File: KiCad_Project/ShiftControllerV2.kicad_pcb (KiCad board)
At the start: 2 copper layers, 20 parts, among them J1 SOLENOID, J2 PWR + I/O, Q1 BTN8982TA, Q2 BTN8982TA, U1 ControllerBoardV1

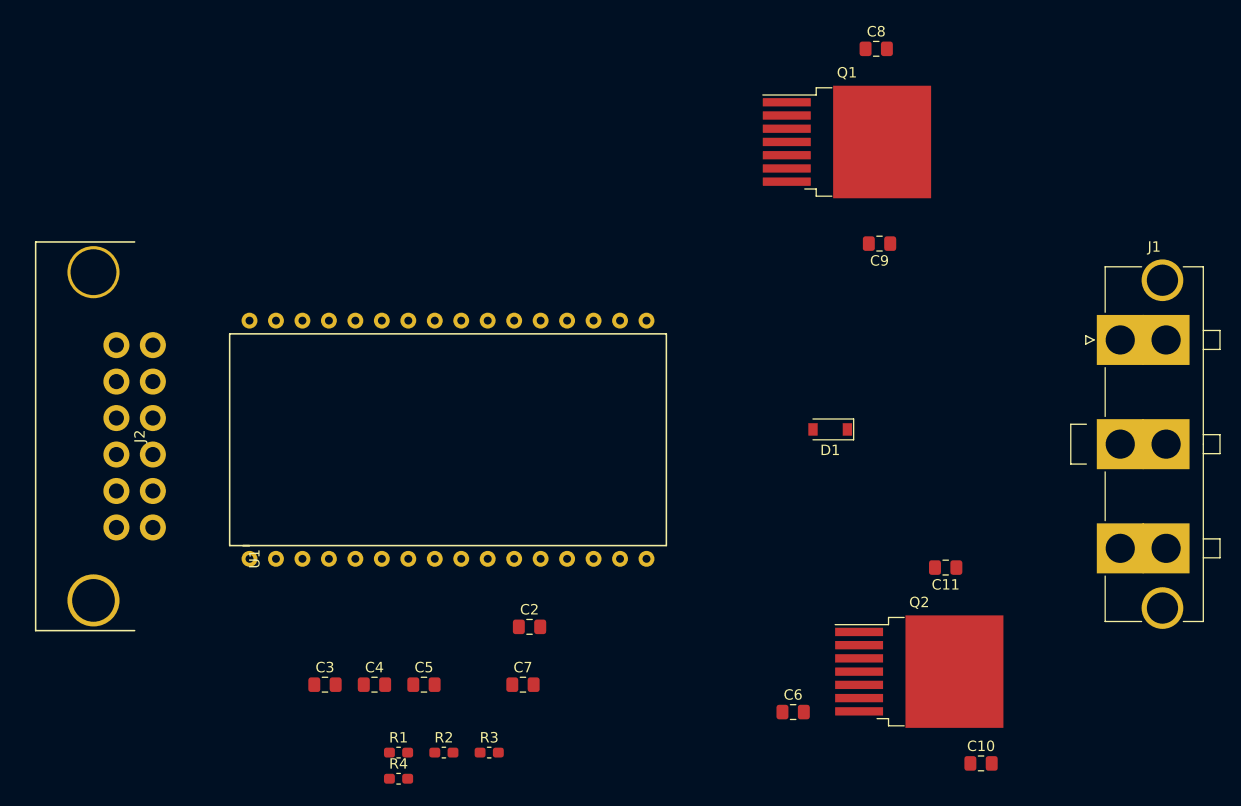
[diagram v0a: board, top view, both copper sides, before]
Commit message: Began planning arrangement of components
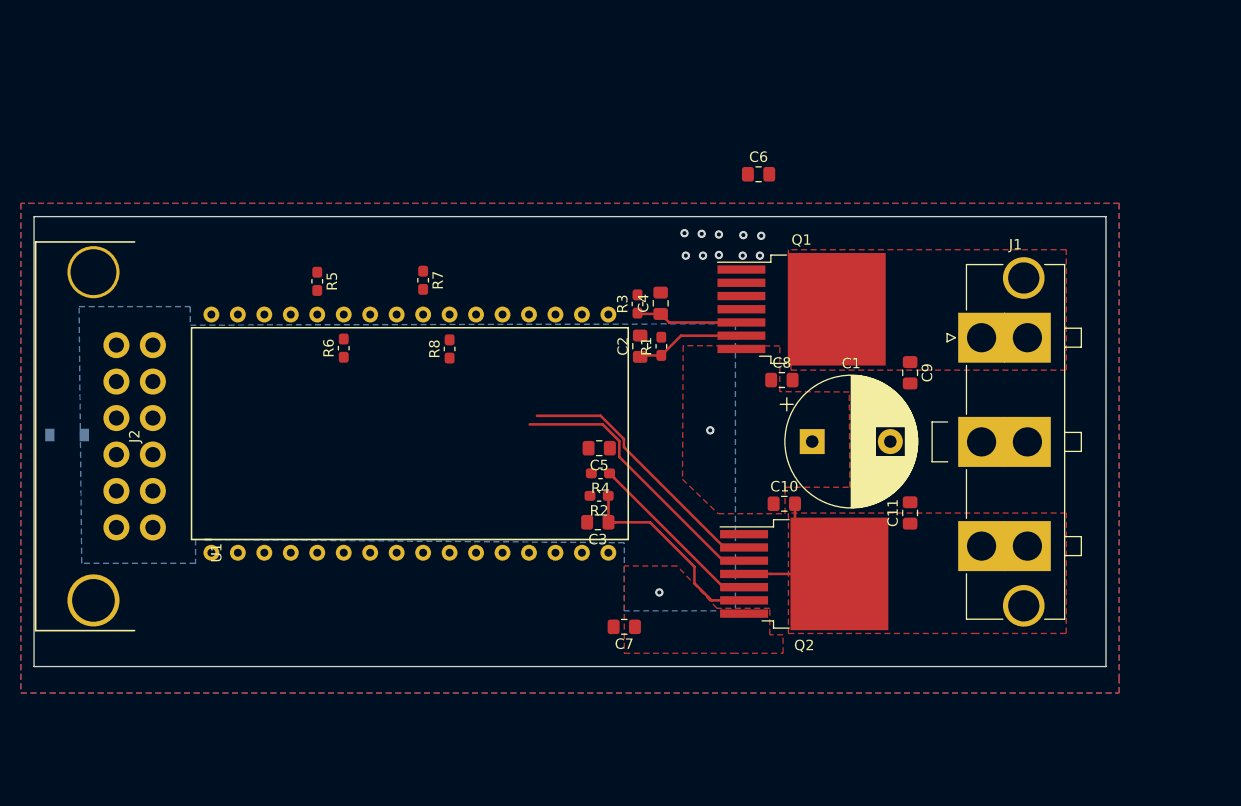
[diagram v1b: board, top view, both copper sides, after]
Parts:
- added C1: 1000u, Capacitor_THT:CP_Radial_D12.5mm_P7.50mm, F.Cu at (150.9, 97.8)
- added R5: 10k, Resistor_SMD:R_0603_1608Metric_Pad1.05x0.95mm_HandSolder, F.Cu at (103.4, 82.4)
- added R6: 10k, Resistor_SMD:R_0603_1608Metric_Pad1.05x0.95mm_HandSolder, F.Cu at (105.9, 88.8)
- added R7: 10k, Resistor_SMD:R_0603_1608Metric_Pad1.05x0.95mm_HandSolder, F.Cu at (113.5, 82.3)
- added R8: 10k, Resistor_SMD:R_0603_1608Metric_Pad1.05x0.95mm_HandSolder, F.Cu at (116.1, 88.9)
- C3: value 100n -> 1n
- D1: value 30v -> 30v zener; moved to B.Cu
- moved D1 73.2 mm to (79.4, 97.2)
- moved C6 51.7 mm to (145.7, 72.1)
- moved R1 46.4 mm to (136.4, 88.6), turned to 90 degrees
- moved C4 45.8 mm to (136.3, 84.5), turned to 90 degrees
- moved R3 45.3 mm to (134.1, 84.6), turned to 90 degrees
- moved R4 35.1 mm to (130.6, 100.8), turned to 180 degrees
- moved C8 33.1 mm to (148.0, 91.9)
- moved C10 31.3 mm to (148.2, 103.8)
- moved C3 30.5 mm to (130.3, 105.5), turned to 180 degrees
- moved C2 29.0 mm to (134.4, 88.6), turned to 90 degrees
- moved R2 28.8 mm to (130.4, 103.0), turned to 180 degrees
- moved C5 28.2 mm to (130.4, 98.4), turned to 180 degrees
- moved Q1 16.6 mm to (149.9, 85.1)
- moved Q2 14.5 mm to (150.1, 110.5)
- moved J1 13.3 mm to (167.1, 87.8)
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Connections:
- J2 pad 3: CANH -> CANL
- J2 pad 4: CANL -> CANH
- Q1 pad 2: (no net) -> IN1
- Q1 pad 3: (no net) -> INH1
- Q2 pad 2: (no net) -> IN2
- Q2 pad 3: (no net) -> INH2
- U1 pad 21: (no net) -> Net-(R5-Pad2)
- U1 pad 22: (no net) -> Net-(R6-Pad2)
- U1 pad 23: CURRENT1 -> CURRENT2
- U1 pad 24: CURRENT2 -> CURRENT1
- U1 pad 25: (no net) -> Net-(R7-Pad2)
- U1 pad 26: (no net) -> Net-(R8-Pad2)
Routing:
- net INH2: track 0.00 -> 26.9 mm
- net IN2: track 0.00 -> 25.6 mm
- net CURRENT2: track 0.00 -> 19.6 mm
- net OUT2: track 0.00 -> 17.6 mm
- net Net-(C5-Pad1): track 0.00 -> 17.4 mm
- net CURRENT1: track 0.00 -> 10.6 mm
- net Net-(C4-Pad1): track 0.00 -> 10.3 mm
- net INH1: track 0.00 -> 1.90 mm
- net IN1: track 0.00 -> 1.90 mm
- net GND: vias 0 -> 10
- net +12V: vias 0 -> 2
- added copper zone on B.Cu, net +12V
- added copper zone on F.Cu, net +12V
- added copper zone on B.Cu, net GND
- added copper zone on F.Cu, net GND
- added copper zone on F.Cu, net OUT1
- added copper zone on F.Cu, net OUT2
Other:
- board outline added: 102.9 x 43.2 mm

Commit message: Layout almost complete
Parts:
- removed C2: 1n, Capacitor_SMD:C_0805_2012Metric_Pad1.15x1.40mm_HandSolder
- added Ce: 1n, Capacitor_SMD:C_0603_1608Metric_Pad1.05x0.95mm_HandSolder, F.Cu at (135.5, 81.3)
- C10, C11, C3, C4, C5, C6, C7, C8, C9: footprint Capacitor_SMD:C_0805_2012Metric_Pad1.15x1.40mm_HandSolder -> Capacitor_SMD:C_0603_1608Metric_Pad1.05x0.95mm_HandSolder
- D1: moved to F.Cu
- J1: value SOLENOID -> Conn_02x06_Top_Bottom; footprint Connector_Molex:Molex_Mini-Fit_Sr_42819-32XX_1x03_P10.00mm_Vertical -> Lukas_Library:MX120G
- J2: value PWR + I/O -> Conn_02x06_Top_Bottom
- R5, R6, R7, R8: moved to B.Cu
- moved C6 16.4 mm to (135.4, 85.0), turned to 180 degrees
- moved D1 14.8 mm to (90.8, 87.7), turned to 135 degrees
- moved C5 13.4 mm to (135.1, 111.0)
- moved R2 13.0 mm to (135.4, 115.1)
- moved J1 11.7 mm to (173.2, 97.8), turned to 270 degrees
- moved R4 9.51 mm to (135.3, 109.1)
- moved C3 9.01 mm to (135.1, 113.2)
- moved R7 7.24 mm to (113.5, 89.5), turned to 90 degrees
- moved R5 7.11 mm to (103.4, 89.5), turned to 90 degrees
- moved R3 7.05 mm to (135.5, 77.7), turned to 180 degrees
- moved C11 5.88 mm to (165.1, 101.3)
- moved C9 5.74 mm to (165.1, 94.3)
- moved R1 5.66 mm to (135.5, 83.1), turned to 180 degrees
- moved Q1 5.36 mm to (153.0, 80.8)
- moved C4 5.08 mm to (135.5, 79.5), turned to 180 degrees
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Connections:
- J1 pad 1: OUT1 -> OUT2
- J1 pad 2: GND -> OUT2
- J1 pad 3: OUT2 -> GND
- J2 pad 1: +12V -> GND
- J2 pad 11: GND -> (no net)
- J2 pad 12: +12V -> GND
- J2 pad 2: GND -> +12V
- J2 pad 3: CANL -> +12V
- J2 pad 4: CANH -> +12V
- J2 pad 5: GND -> +12V
- J2 pad 6: +12V -> GND
- J2 pad 7: +12V -> GND
- J2 pad 8: GND -> CANH
- J2 pad 9: (no net) -> CANL
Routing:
- net INH1: track 1.90 -> 50.1 mm, vias 0 -> 1
- net CURRENT1: track 10.6 -> 49.9 mm, vias 0 -> 1
- net IN1: track 1.90 -> 40.6 mm, vias 0 -> 1
- net CURRENT2: track 19.6 -> 56.5 mm, vias 0 -> 1
- net INH2: track 26.9 -> 51.0 mm, vias 0 -> 1
- net IN2: track 25.6 -> 48.4 mm, vias 0 -> 1
- net CANL: track 0.00 -> 17.9 mm
- net GND: track 0.00 -> 15.2 mm, vias 10 -> 47
- net CANH: track 0.00 -> 14.2 mm
- net OUT1: track 0.00 -> 9.15 mm, vias 0 -> 9
- net OUT2: track 17.6 -> 9.15 mm, vias 0 -> 9
- net Net-(C4-Pad1): track 10.3 -> 13.7 mm
- net Net-(C5-Pad1): track 17.4 -> 14.7 mm
- net Net-(R7-Pad2): track 0.00 -> 2.31 mm
- net Net-(R6-Pad2): track 0.00 -> 2.30 mm
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- added copper zone on B.Cu, net OUT1
- added copper zone on B.Cu, net OUT2
- removed copper zone on B.Cu, net +12V
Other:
- board size 102.9 x 43.2 mm -> 106.7 x 58.4 mm
- net class Default: clearance 0.2 -> 0.1524; trace_width 0.25 -> 0.1524; via_dia 0.8 -> 0.381; via_drill 0.4 -> 0.3048
- net class Power added: clearance 0.254, trace_width 0.762, via_dia 0.635, via_drill 0.381
- rule trace_clearance: 0.2 -> 0.1524
- rule trace_min: 0.2 -> 0.1524
- rule via_min_drill: 0.3 -> 0.2794
- rule via_min_size: 0.4 -> 0.381

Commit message: V1 Complete and out for manufacturing
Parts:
- added G***: LOGO, Lukas_Library:UBCOLogo, F.Cu at (109.4, 120.5)
- moved C7 1.56 mm to (130.3, 114.4)
- moved R2 0.81 mm to (135.1, 114.3)
- moved C3 0.64 mm to (135.1, 112.5)
- moved C5 0.25 mm to (135.1, 110.7)
- moved R4 0.20 mm to (135.1, 108.9)
- moved C8 0.19 mm to (150.9, 88.6)
- renumbered Ce to C2
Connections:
- J1 pad 13: (no net) -> OUT1
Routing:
- net GND: track 15.2 -> 0.00 mm, vias 47 -> 49
- net CURRENT1: track 49.9 -> 48.6 mm
- net CURRENT2: track 56.5 -> 55.6 mm
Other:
- board text added: "LV 01/2020"
- board text added: "SHIFT CONTROLLER V2.0"
